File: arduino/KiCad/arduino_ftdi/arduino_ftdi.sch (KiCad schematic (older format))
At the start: 21 parts, among them J1 RJ45, J10 9V-12V, J11 3V3 & 5V, J12 9V-12V, J13 3V3 & 5V, J2 IN/OUT, J3 RTS/TX/RX, J4 Power output 3V3, J5 NC, J6 RTS, J7 TX, J8 RX, J9 Power input 9V-12V, U1 MAX488E, U2 MAX488E, U3 TXB0104 breakout (SparkFun BO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

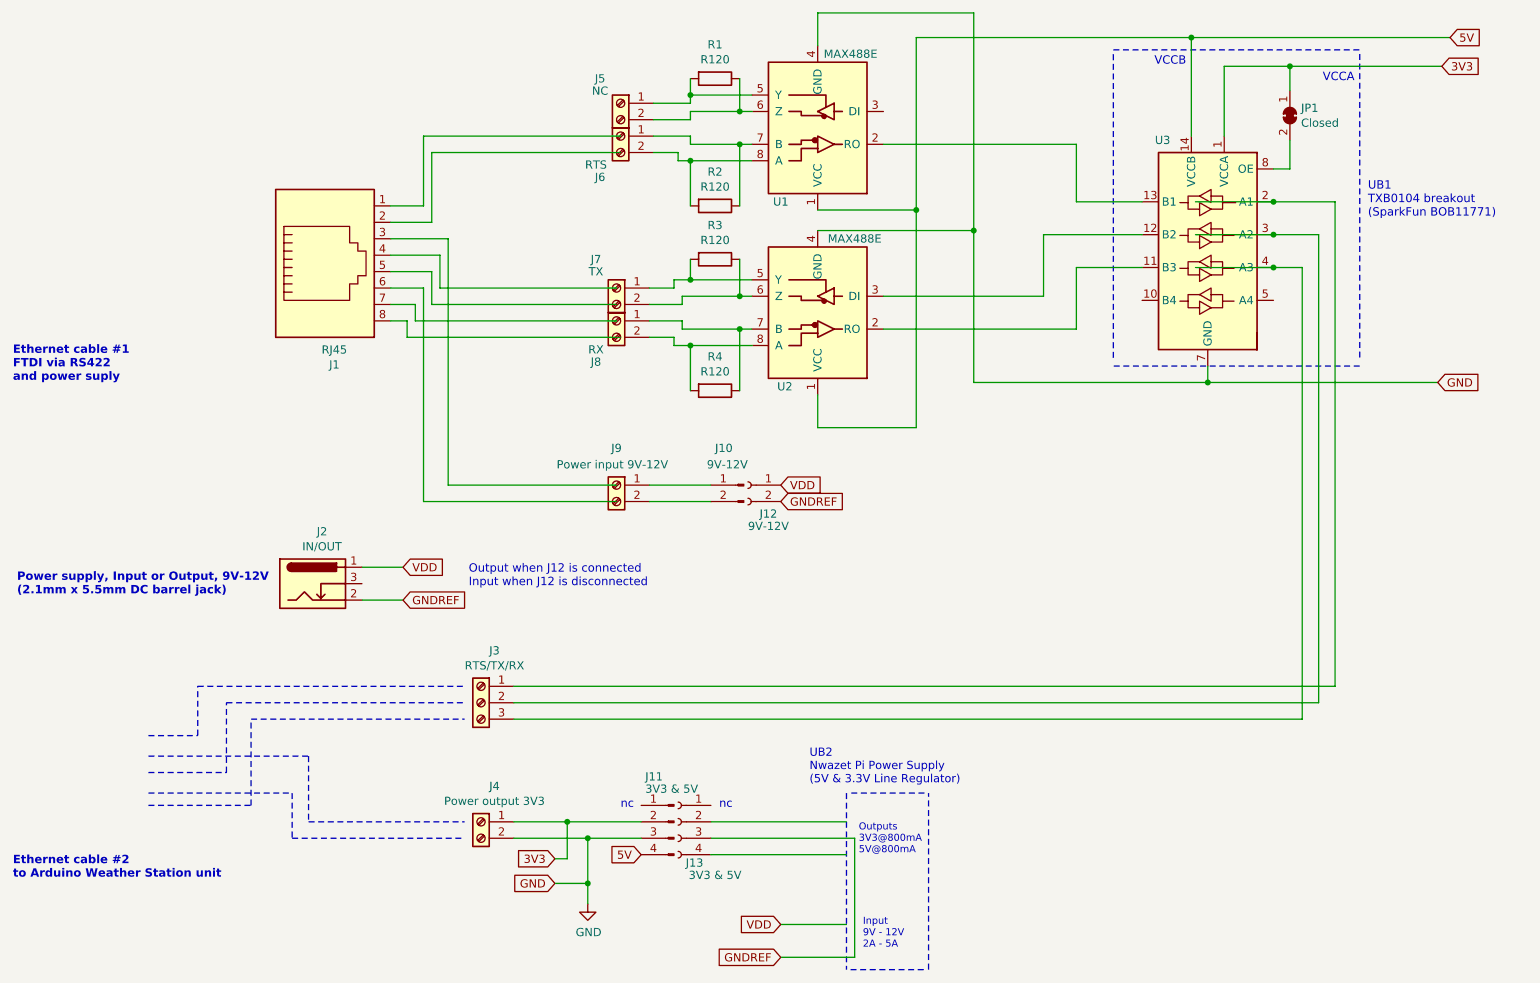
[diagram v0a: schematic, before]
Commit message: Updated RS422 to UART schematics. Add UART to RS422 schematics
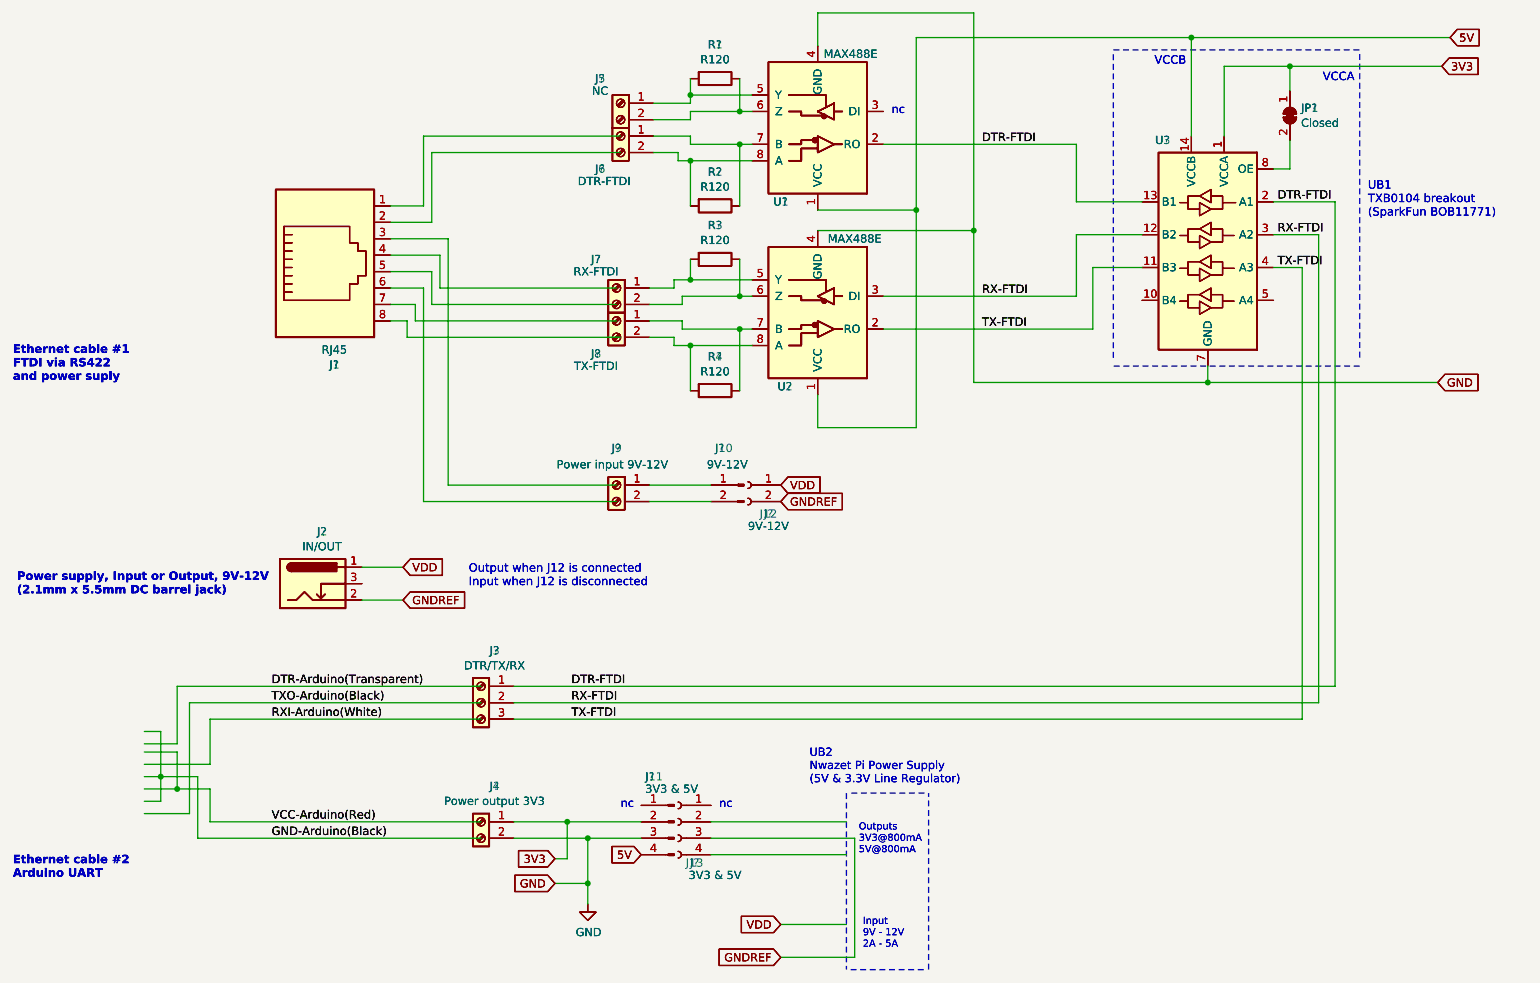
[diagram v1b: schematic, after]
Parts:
- added J1: RJ45, symbol Connector:RJ45
- added J11: 3V3 & 5V, symbol Connector:Conn_01x04_Male
- added J12: 9V-12V, symbol Connector:Conn_01x02_Female
- added J13: 3V3 & 5V, symbol Connector:Conn_01x04_Female
- added J3: DTR/TX/RX, symbol Connector:Screw_Terminal_01x03
- added J9: Power input 9V-12V, symbol Connector:Screw_Terminal_01x02
- added J?: IN/OUT, symbol Connector:Barrel_Jack_Switch
- added J?: Power output 3V3, symbol Connector:Screw_Terminal_01x02
- added J?: NC, symbol Connector:Screw_Terminal_01x02
- added J?: DTR-FTDI, symbol Connector:Screw_Terminal_01x02
- added J?: RX-FTDI, symbol Connector:Screw_Terminal_01x02
- added J?: TX-FTDI, symbol Connector:Screw_Terminal_01x02
- added J?: 9V-12V, symbol Connector:Conn_01x02_Male
- added JP1: Closed, symbol Jumper:SolderJumper_2_Bridged
- added R1, R2, R3, R4: R120, symbol Device:R
- added U1, U?: MAX488E, symbol Interface_UART:MAX488E
- added U3: TXB0104 breakout (SparkFun BOB11771), Package_SO:SOIC-14_3.9x8.7mm_P1.27mm, symbol Logic_LevelTranslator:TXB0104D
- J6: value RTS -> DTR-FTDI
- J7: value TX -> RX-FTDI
- J8: value RX -> TX-FTDI
- J?: renamed from J3; value RTS/TX/RX -> DTR/TX/RX
- renumbered J1 to J?, J9 to J?, J11 to J?, J12 to J?, J13 to J?, JP1 to JP?, R1 to R?, R2 to R?, R3 to R?, R4 to R?, U1 to U?, U3 to U?
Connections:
- net labels added: DTR-Arduino(Transparent), DTR-FTDI, GND-Arduino(Black), RX-FTDI, RXI-Arduino(White), TX-FTDI, TXO-Arduino(Black), VCC-Arduino(Red)
- wire segments 125 -> 145
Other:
- note added: "Ethernet cable #2\nArduino UART"
- note removed: "Ethernet cable #2\nto Arduino Weather Station unit"

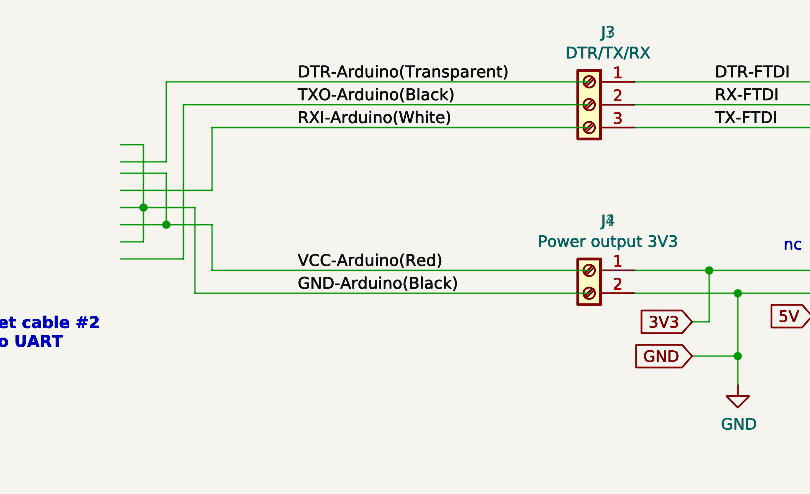
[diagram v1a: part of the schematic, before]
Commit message: Correct color of the GND wire to Arduino
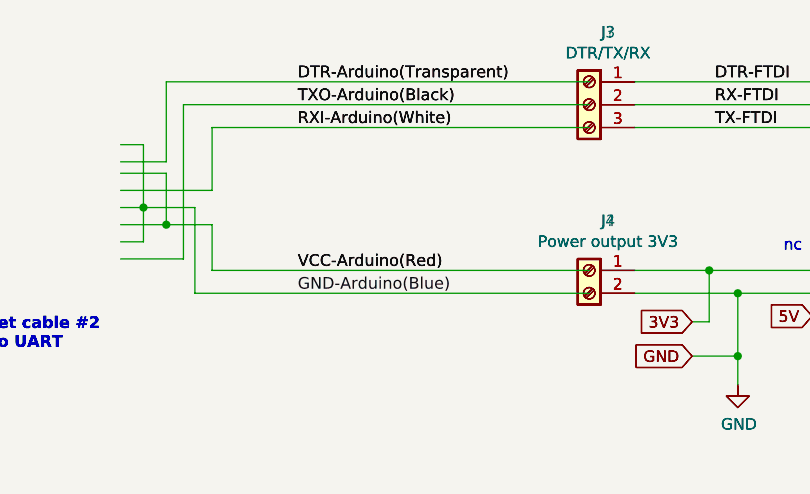
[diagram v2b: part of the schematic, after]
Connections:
- net labels added: GND-Arduino(Blue)
- net labels removed: GND-Arduino(Black)
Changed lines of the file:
@@
 Sheet 1 1
 Title "RS422 5V to UART 3V3 interface"
-Date "2020-09-16"
-Rev "2.1"
+Date "2020-09-28"
+Rev "2.2"
 Comp ""
 Comment1 "Interface to provide UART from RS442 on Ethernet cable"
@@
 Text Label 2700 5800 0    51   ~ 0
 VCC-Arduino(Red)
-Text Label 2700 5900 0    51   ~ 0
-GND-Arduino(Black)
 Wire Wire Line
 	1925 5450 2325 5450
@@
 VCC-Arduino(Red)
 Text Label 2700 5900 0    51   ~ 0
-GND-Arduino(Black)
+GND-Arduino(Blue)
 Text Label 2700 4975 0    51   ~ 0
 DTR-Arduino(Transparent)
